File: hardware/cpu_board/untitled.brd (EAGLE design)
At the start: 126.3 x 94.6 mm, 74 parts, among them IC1 MAX232ECWE, IC2 MAX232ECWE, IC3 AM29F040J, IC4 74HCT138D, IC5 LM2596S, IC6 74HCT273DW, IC8 74LVC1G04DBV, J2 POWER_JACKSLT, U1 AS6C4008-55SIN

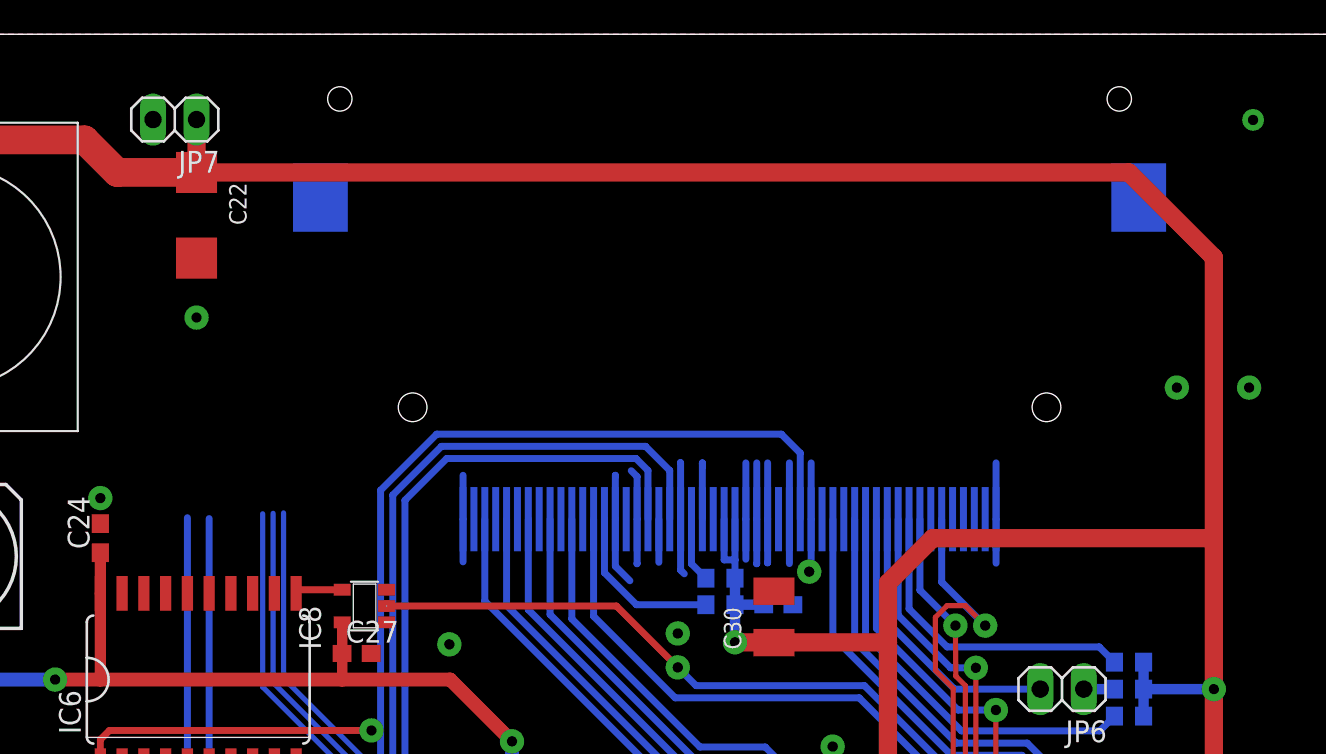
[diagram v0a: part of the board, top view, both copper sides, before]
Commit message: VCC rerouted
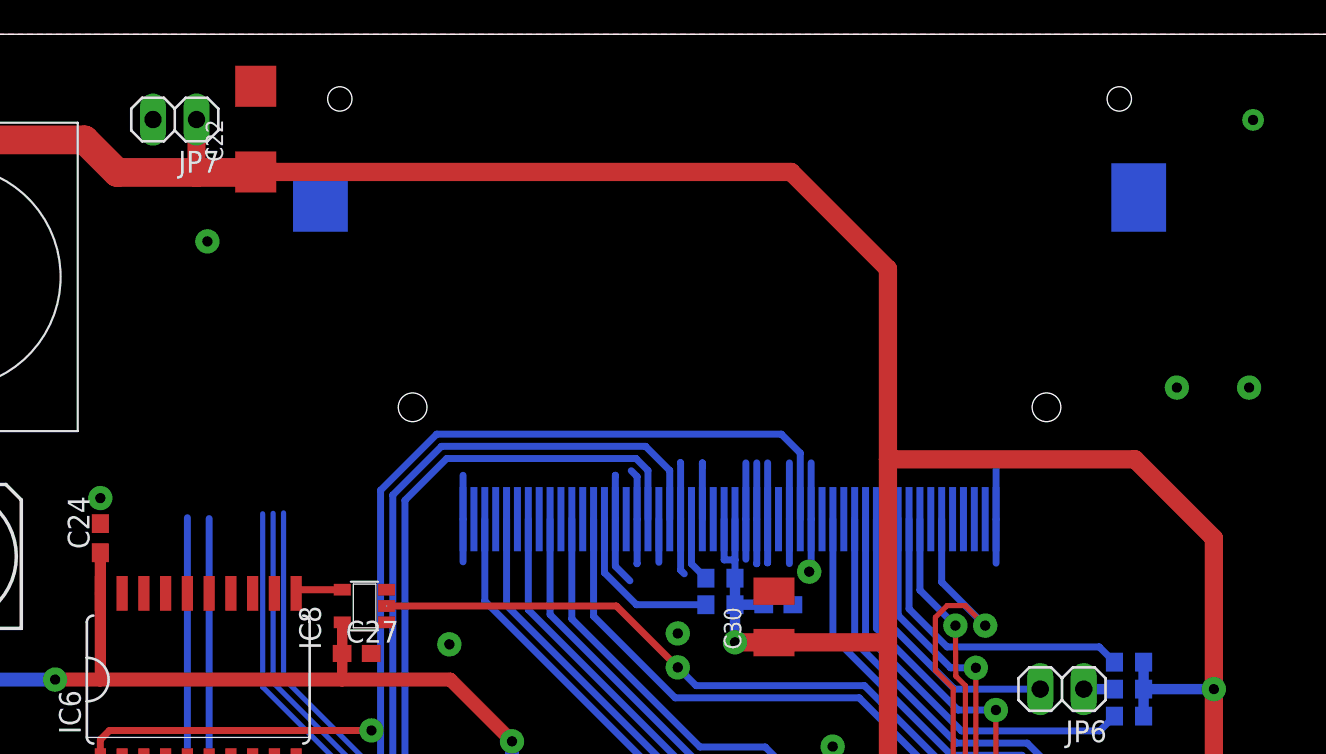
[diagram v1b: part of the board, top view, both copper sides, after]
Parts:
- moved C22 6.10 mm to (63.1, 89.1), turned to 90 degrees
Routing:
- net 5V: track 503.6 -> 487.6 mm
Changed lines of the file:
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@@
 <element name="L2" library="mw" package="NIX_CHOKE_SMD" value="NIX_CHOKE_SMD" x="52.7558" y="71.4502" rot="R90"/>
 <element name="JP7" library="pinhead" package="1X02" value="" x="58.42" y="89.6366" rot="R180"/>
-<element name="C22" library="rcl" package="SMC_C" value="" x="59.69" y="84.0486" rot="R270"/>
+<element name="C22" library="rcl" package="SMC_C" value="" x="63.1444" y="89.0778" rot="R90"/>
 <element name="JP8" library="pinhead" package="1X02" value="" x="19.685" y="79.97"/>
 <element name="C24" library="rcl" package="C0603" value="" x="54.0766" y="65.2018" rot="R90"/>
@@
 <contactref element="JP7" pad="2"/>
 <contactref element="C22" pad="-"/>
-<via x="59.69" y="78.0796" extent="1-16" drill="0.6" diameter="1.4224" shape="octagon"/>
+<via x="60.325" y="82.5246" extent="1-16" drill="0.6" diameter="1.4224" shape="octagon"/>
 <via x="31.115" y="86.3346" extent="1-16" drill="0.6" diameter="1.4224" shape="octagon"/>
 <via x="75.9206" y="48.4124" extent="1-16" drill="0.6" diameter="1.4224" shape="octagon"/>
@@
 <wire x1="27.305" y1="72.39" x2="31.3182" y2="72.39" width="0.8128" layer="1"/>
 <contactref element="JP7" pad="1"/>
-<wire x1="59.69" y1="86.5452" x2="59.69" y2="86.5486" width="1.0668" layer="1"/>
 <contactref element="C22" pad="+"/>
-<wire x1="59.69" y1="86.5486" x2="59.69" y2="89.6366" width="1.0668" layer="1"/>
 <wire x1="24.13" y1="41.0718" x2="27.7994" y2="44.7412" width="0.8128" layer="16"/>
 <wire x1="27.7994" y1="56.9468" x2="27.7994" y2="60.4656" width="0.8128" layer="16"/>
@@
 <via x="91.1216" y="59.1194" extent="1-16" drill="0.6" diameter="1.4224" shape="octagon"/>
 <wire x1="32.131" y1="56.9468" x2="51.435" y2="56.9468" width="0.8128" layer="16"/>
-<wire x1="114.1114" y1="86.5486" x2="119.0752" y2="81.5848" width="1.0668" layer="1"/>
+<wire x1="94.3972" y1="86.5778" x2="100.0506" y2="80.9244" width="1.0668" layer="1"/>
 <wire x1="119.0752" y1="56.388" x2="119.0752" y2="65.20024375" width="1.0668" layer="1"/>
-<wire x1="119.0752" y1="65.20024375" x2="119.0752" y2="81.5848" width="1.0668" layer="1"/>
 <wire x1="91.1216" y1="59.1194" x2="93.345" y2="59.1194" width="1.0668" layer="1"/>
 <wire x1="93.345" y1="59.1194" x2="100.0506" y2="59.1194" width="1.0668" layer="1"/>
 <wire x1="100.0506" y1="59.1194" x2="100.0506" y2="50.8" width="1.0668" layer="1"/>
-<wire x1="119.0752" y1="65.20024375" x2="102.66524375" y2="65.20024375" width="1.0668" layer="1"/>
-<wire x1="102.66524375" y1="65.20024375" x2="100.0506" y2="62.5856" width="1.0668" layer="1"/>
-<wire x1="100.0506" y1="59.1194" x2="100.0506" y2="62.5856" width="1.0668" layer="1"/>
 <contactref element="C24" pad="1"/>
 <contactref element="C26" pad="1"/>
@@
 <wire x1="45.2558" y1="88.4502" x2="53.1548" y2="88.4502" width="1.6764" layer="1"/>
 <wire x1="53.1548" y1="88.4502" x2="55.0564" y2="86.5486" width="1.6764" layer="1"/>
-<wire x1="59.69" y1="86.5486" x2="55.0564" y2="86.5486" width="1.6764" layer="1"/>
 <via x="57.785" y="35.0148" extent="1-16" drill="0.6" diameter="1.4224" shape="octagon"/>
-<wire x1="59.69" y1="86.5486" x2="114.1114" y2="86.5486" width="1.0668" layer="1"/>
 <wire x1="40.2708" y1="36.5896" x2="32.1192" y2="44.7412" width="0.8128" layer="16"/>
 <wire x1="27.7994" y1="44.7412" x2="32.1192" y2="44.7412" width="0.8128" layer="16"/>
@@
 <wire x1="57.785" y1="35.0148" x2="57.785" y2="35.8784" width="0.6096" layer="1"/>
 <wire x1="57.785" y1="35.8784" x2="57.0738" y2="36.5896" width="0.6096" layer="1"/>
+<wire x1="55.0564" y1="86.5486" x2="59.69" y2="86.5486" width="1.6764" layer="1"/>
+<wire x1="59.69" y1="86.5486" x2="63.1152" y2="86.5486" width="1.6764" layer="1"/>
+<wire x1="63.1152" y1="86.5486" x2="63.1444" y2="86.5778" width="1.6764" layer="1"/>
+<wire x1="63.1444" y1="86.5778" x2="94.3972" y2="86.5778" width="1.0668" layer="1"/>
+<wire x1="100.0506" y1="59.1194" x2="100.0506" y2="69.80655" width="1.0668" layer="1"/>
+<wire x1="100.0506" y1="69.80655" x2="100.0506" y2="80.9244" width="1.0668" layer="1"/>
+<wire x1="100.0506" y1="69.80655" x2="114.46889375" y2="69.80655" width="1.0668" layer="1"/>
+<wire x1="114.46889375" y1="69.80655" x2="119.0752" y2="65.20024375" width="1.0668" layer="1"/>
+<wire x1="59.69" y1="89.6366" x2="59.69" y2="86.5486" width="1.0668" layer="1"/>
 <wire x1="28.0162" y1="-10.907" x2="31.75" y2="12.7" width="0" layer="19" extent="1-16"/>
 <wire x1="16.6624" y1="-6.6398" x2="28.0162" y2="-10.907" width="0" layer="19" extent="1-1"/>

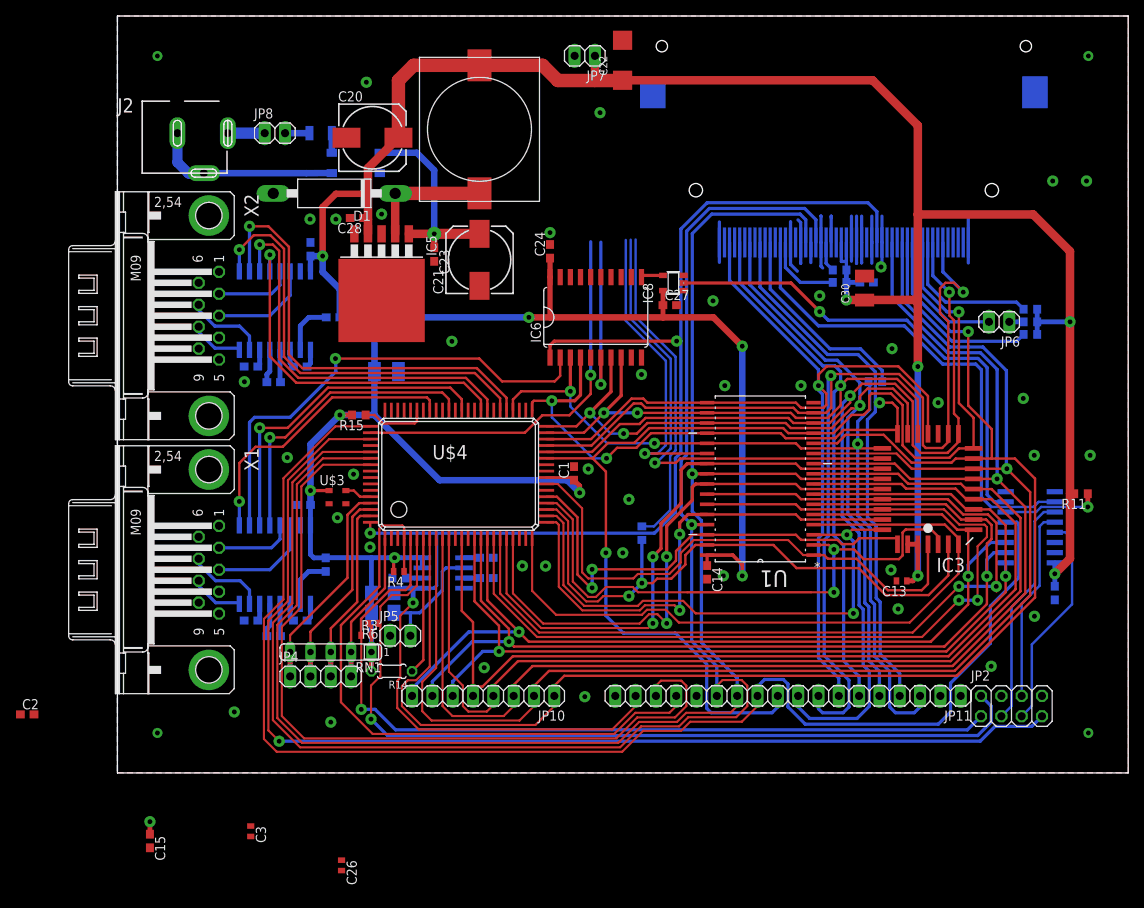
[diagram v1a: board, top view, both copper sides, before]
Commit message: Writing to 273 fixed
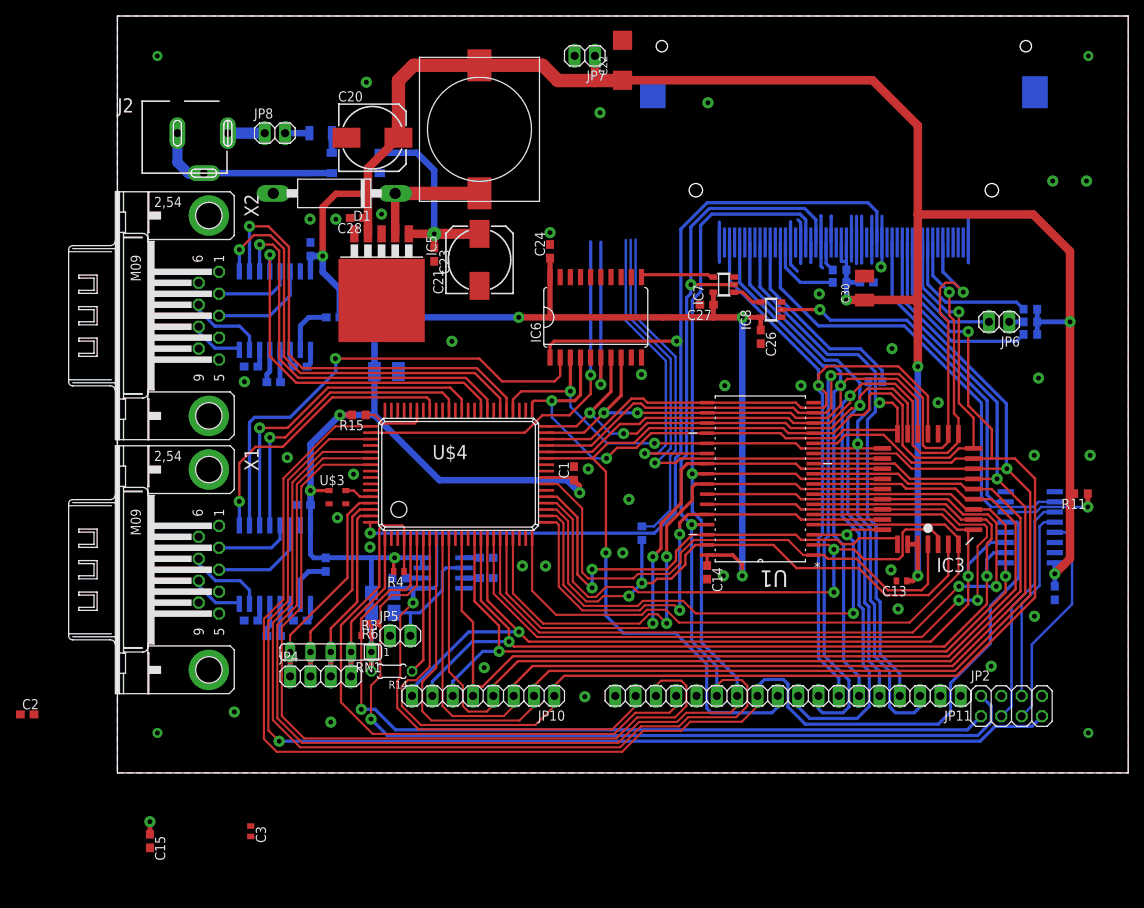
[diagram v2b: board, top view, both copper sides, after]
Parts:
- added IC7: 74LVC1G08DBV, 74xx-little-de:SOT23-5
- C26: device rcl:C0402 -> rcl:C0603
- moved C26 84.3 mm to (80.4, 54.5)
- moved IC8 12.7 mm to (81.7, 57.9)
- moved C27 4.62 mm to (73.7, 58.5), turned to 180 degrees
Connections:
- new net N$45: IC7.1, IC8.4
- net !WR: now also IC7.2
- net 5V: now also IC7.5
- net GND: now also IC7.3
- net N$44: now also IC7.4; no longer IC8.4
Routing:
- net LOCAL_PORT_CS: track 60.9 -> 44.9 mm
- net N$44: track 2.89 -> 9.41 mm
- net 5V: track 487.6 -> 493.5 mm
- net !WR: track 196.1 -> 201.5 mm, vias 1 -> 2
- net N$45: track 0.00 -> 3.84 mm
- net CF_CS0: track 60.9 -> 58.5 mm
- net A1: track 184.9 -> 182.4 mm
- net A2: track 179.1 -> 176.7 mm

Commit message: RAM/ROM address decoder (work in progress)
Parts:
- added IC9: 74HCT138D, 74xx-eu:SO16
- added LED1: (no value), led:CHIP-LED0603
- added R17, R18: (no value), rcl:R0603
- moved C24 0.48 mm to (54.1, 64.7)
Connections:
- new net N$46: IC6.9, R17.2
- new net N$47: LED1.A, R17.1
- new net N$48: IC9.6, R18.1
- net !MEMEN: now also IC9.4
- net !RAM_CS: now also IC9.10, IC9.11, IC9.13
- net !ROM_CS: now also IC9.15
- net 5V: now also IC9.16, R18.2
- net GND: now also IC9.1, IC9.5, IC9.8, LED1.C
- net ROMSHADOW: now also IC9.2
- net _A15: now also IC9.3
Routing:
- net !RAM_CS: track 38.6 -> 51.6 mm
- net !ROM_CS: track 59.5 -> 66.9 mm
- net ROMSHADOW: track 21.1 -> 28.0 mm
- net N$46: track 0.00 -> 2.17 mm
- net N$48: track 0.00 -> 1.89 mm
- net N$47: track 0.00 -> 1.49 mm
- net !MEMEN: track 48.5 -> 50.0 mm
- net _A15: track 40.6 -> 41.7 mm
- net D6: track 135.6 -> 136.3 mm
- net GND: vias 39 -> 40

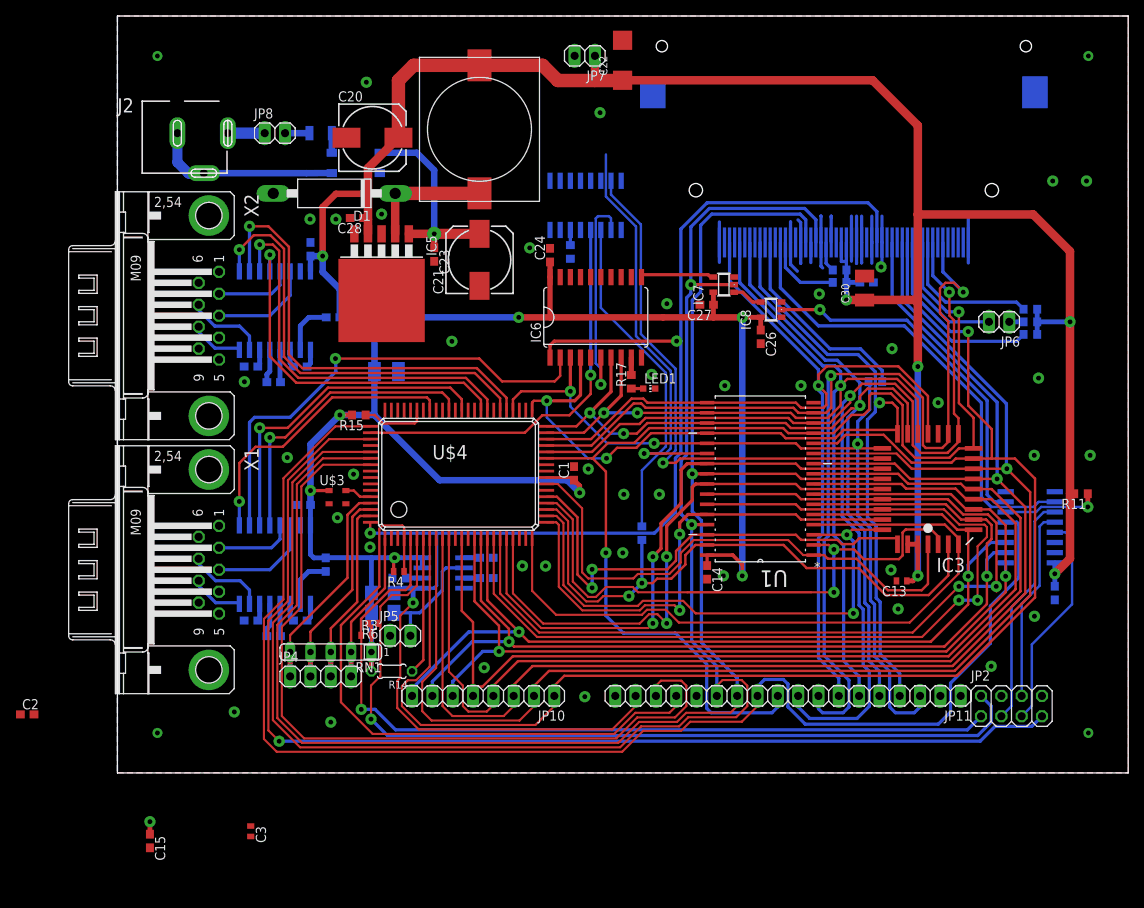
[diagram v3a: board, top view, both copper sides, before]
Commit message: ROM/RAM address decoder (version with diodes and wired-or on RAMCS line)
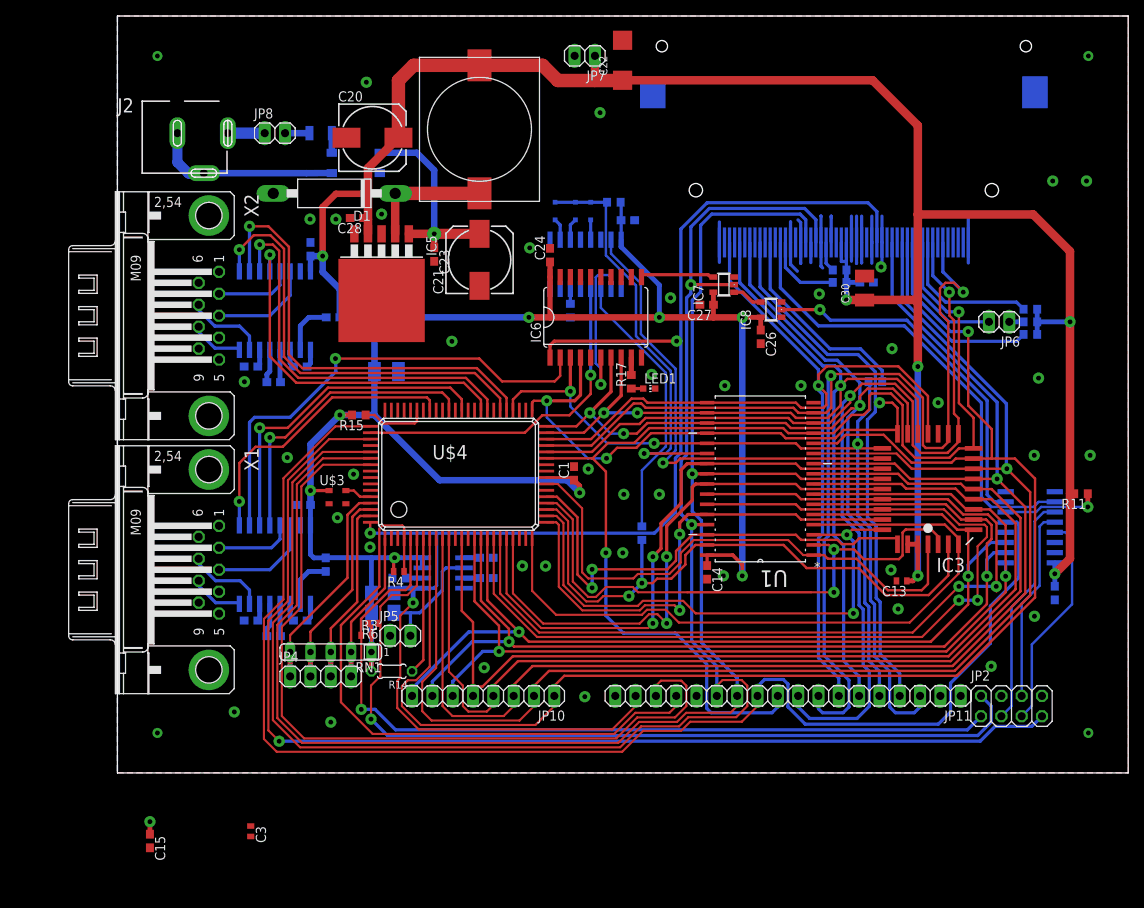
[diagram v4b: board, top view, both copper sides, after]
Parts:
- added D2, D3, D4: (no value), adafruit:SOD-323
- added R19: (no value), rcl:R0603
- moved C2 97.2 mm to (63.8, 69.1), flipped to the bottom, turned to 180 degrees
- moved IC9 7.37 mm to (58.5, 63.6)
- moved R18 7.34 mm to (56.6, 57.8)
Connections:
- new net N$49: D2.C, IC9.13
- new net N$50: D4.C, IC9.10
- new net N$51: D3.C, IC9.11
- net !RAM_CS: now also D2.A, D3.A, D4.A, R19.1; no longer IC9.10, IC9.11, IC9.13
- net 5V: now also R19.2
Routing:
- net 5V: track 493.0 -> 514.9 mm, vias 14 -> 15
- net ROMSHADOW: track 28.0 -> 20.6 mm
- net _A15: track 41.7 -> 34.3 mm
- net !ROM_CS: track 66.9 -> 59.5 mm
- net !MEMEN: track 50.0 -> 42.7 mm
- net N$51: track 0.00 -> 2.74 mm
- net N$50: track 0.00 -> 2.74 mm
- net N$49: track 0.00 -> 2.48 mm
- net !RAM_CS: track 51.6 -> 52.1 mm
